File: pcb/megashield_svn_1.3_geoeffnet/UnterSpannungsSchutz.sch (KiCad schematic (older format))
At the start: 15 parts, among them P20 Button, Q3 IRF9540N, Q4 BC337

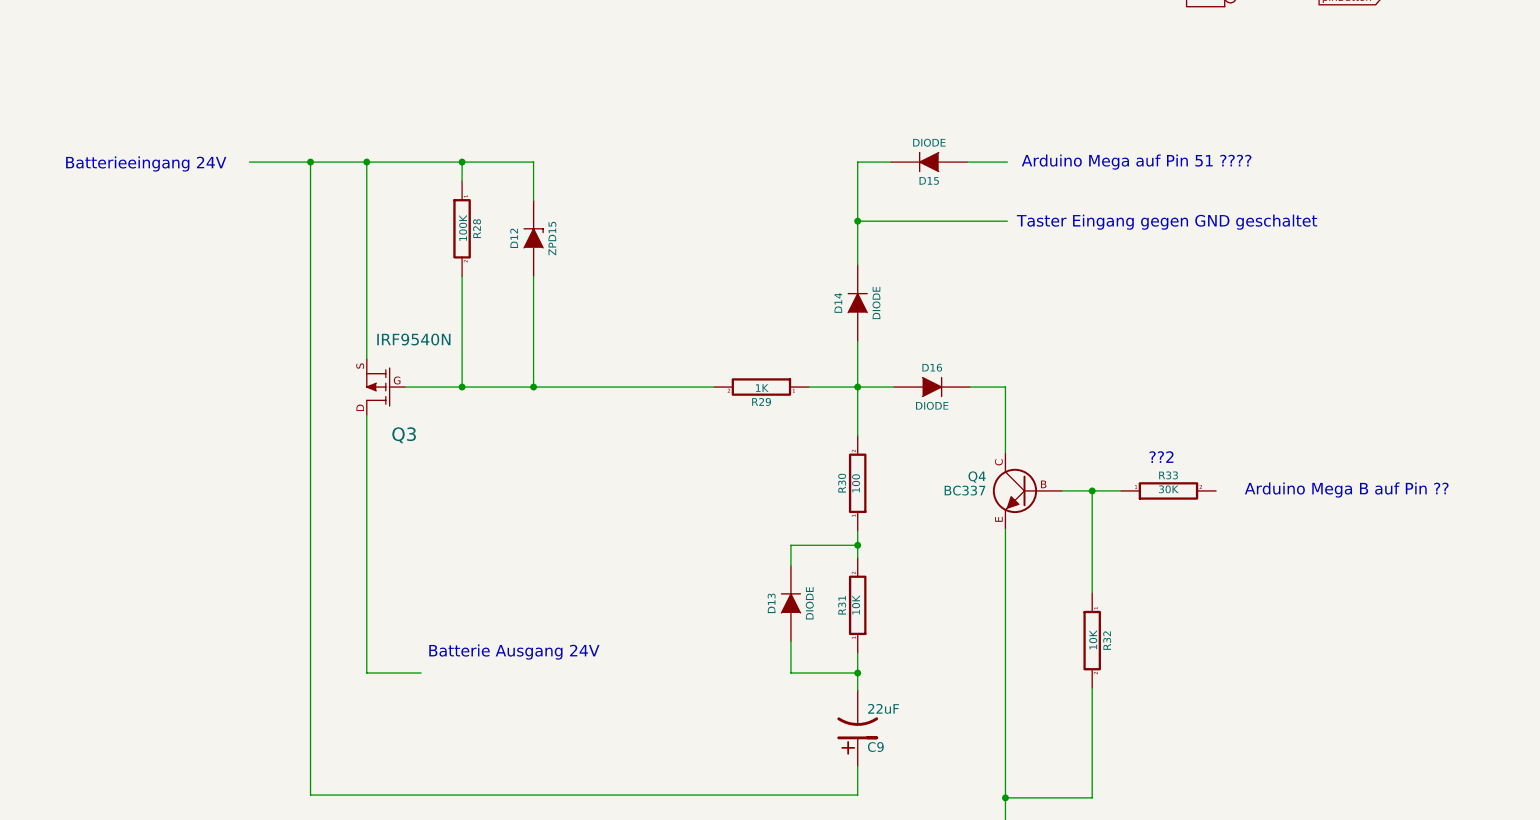
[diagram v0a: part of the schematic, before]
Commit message: Platine V1.3
Hierarchischer Schaltplan für Step Down Wandler erstellt
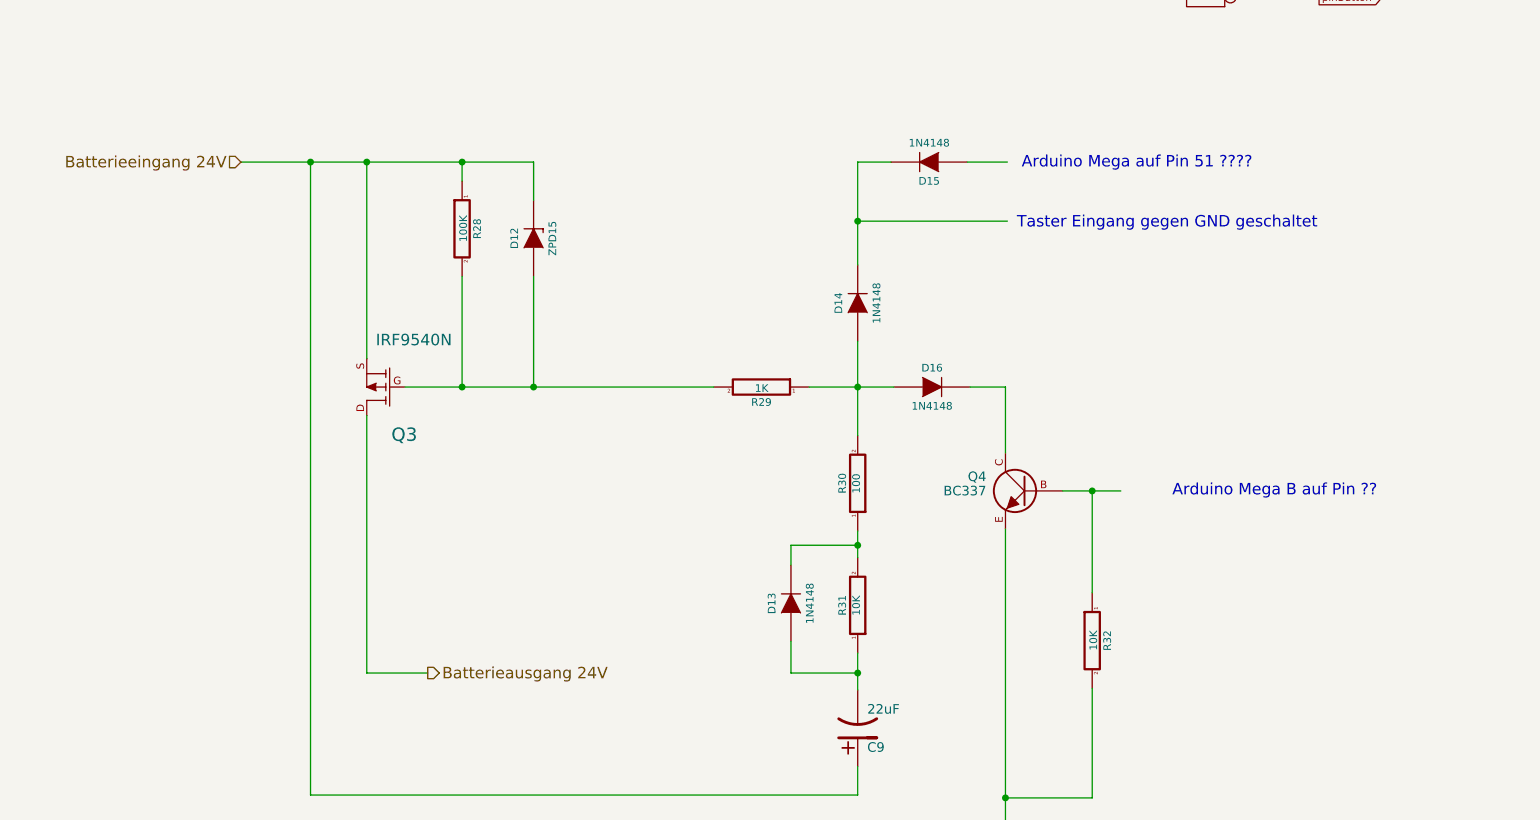
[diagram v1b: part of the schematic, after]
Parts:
- removed R33: 30K, symbol R
- D13, D14, D15, D16: value DIODE -> 1N4148
- P20: footprint (none) -> ACS712:Pin_Header_Straight_1x02
- Q4: footprint TO-92 -> (none)
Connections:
- net labels added: Batterieausgang 24V, Batterieeingang 24V
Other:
- note removed: "??2"
- note removed: "Batterie Ausgang 24V"
- note removed: "Batterieeingang 24V"
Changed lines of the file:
@@
 EESchema Schematic File Version 2
+LIBS:Lötpad_2,5mm
 LIBS:power
 LIBS:Bluetooth_ZS_HC_05
@@
 $Descr A4 11693 8268
 encoding utf-8
-Sheet 3 16
+Sheet 3 17
 Title "Ardumower shield SVN Version 1.3"
 Date "Sonntag, 26. April 2015"
 Rev "1.3"
-Comp " by UweZ"
-Comment1 ""
+Comp "von UweZ"
+Comment1 "Unterspannungsschutz von AlexanderG"
 Comment2 ""
 Comment3 ""
@@
 F 0 "Q3" H 4173 3470 70  0000 C CNN
 F 1 "IRF9540N" H 4123 2973 60  0000 C CNN
-F 2 "" H 4270 3220 60  0000 C CNN
+F 2 "" H 4270 3220 60  0001 C CNN
 F 3 "" H 4270 3220 60  0000 C CNN
 	1    4270 3220
@@
 F 0 "R28" V 4750 2390 40  0000 C CNN
 F 1 "100K" V 4677 2391 40  0000 C CNN
-F 2 "" V 4600 2390 30  0000 C CNN
+F 2 "" V 4600 2390 30  0001 C CNN
 F 3 "" H 4670 2390 30  0000 C CNN
 F 4 "Value" H 4670 2390 60  0001 C CNN "Bestellnummer"
@@
 F 0 "D12" H 5045 2540 40  0000 C CNN
 F 1 "ZPD15" H 5045 2340 40  0000 C CNN
-F 2 "" H 5045 2440 60  0000 C CNN
+F 2 "" H 5045 2440 60  0001 C CNN
 F 3 "" H 5045 2440 60  0000 C CNN
 	1    5045 2440
@@
 F 0 "R29" V 6320 3220 40  0000 C CNN
 F 1 "1K" V 6247 3221 40  0000 C CNN
-F 2 "" V 6170 3220 30  0000 C CNN
+F 2 "" V 6170 3220 30  0001 C CNN
 F 3 "" H 6240 3220 30  0000 C CNN
 F 4 "Value" H 6240 3220 60  0001 C CNN "Bestellnummer"
@@
 P 6745 2780
 F 0 "D14" H 6745 2880 40  0000 C CNN
-F 1 "DIODE" H 6745 2680 40  0000 C CNN
-F 2 "" H 6745 2780 60  0000 C CNN
+F 1 "1N4148" H 6745 2680 40  0000 C CNN
+F 2 "" H 6745 2780 60  0001 C CNN
 F 3 "" H 6745 2780 60  0000 C CNN
 	1    6745 2780
@@
 P 7135 3220
 F 0 "D16" H 7135 3320 40  0000 C CNN
-F 1 "DIODE" H 7135 3120 40  0000 C CNN
-F 2 "" H 7135 3220 60  0000 C CNN
+F 1 "1N4148" H 7135 3120 40  0000 C CNN
+F 2 "" H 7135 3220 60  0001 C CNN
 F 3 "" H 7135 3220 60  0000 C CNN
 	1    7135 3220
@@
 P 7120 2040
 F 0 "D15" H 7120 2140 40  0000 C CNN
-F 1 "DIODE" H 7120 1940 40  0000 C CNN
-F 2 "" H 7120 2040 60  0000 C CNN
+F 1 "1N4148" H 7120 1940 40  0000 C CNN
+F 2 "" H 7120 2040 60  0001 C CNN
 F 3 "" H 7120 2040 60  0000 C CNN
 	1    7120 2040
@@
 F 0 "R30" V 6825 3725 40  0000 C CNN
 F 1 "100" V 6752 3726 40  0000 C CNN
-F 2 "" V 6675 3725 30  0000 C CNN
+F 2 "" V 6675 3725 30  0001 C CNN
 F 3 "" H 6745 3725 30  0000 C CNN
 	1    6745 3725
@@
 F 0 "Q4" H 7820 3840 50  0000 L CNN
 F 1 "BC337" H 7820 3765 50  0000 L CNN
-F 2 "TO-92" H 7820 3690 50  0001 L CIN
+F 2 "" H 7820 3690 50  0001 L CIN
 F 3 "" H 7620 3765 50  0000 L CNN
 	1    7620 3765
 	-1   0    0    -1
-$EndComp
-$Comp
-L R R33
-U 1 1 553A7597
-P 8375 3765
-F 0 "R33" V 8455 3765 40  0000 C CNN
-F 1 "30K" V 8382 3766 40  0000 C CNN
-F 2 "" V 8305 3765 30  0000 C CNN
-F 3 "" H 8375 3765 30  0000 C CNN
-	1    8375 3765
-	0    -1   -1   0
 $EndComp
 $Comp
@@
 F 0 "R32" V 8055 4550 40  0000 C CNN
 F 1 "10K" V 7982 4551 40  0000 C CNN
-F 2 "" V 7905 4550 30  0000 C CNN
+F 2 "" V 7905 4550 30  0001 C CNN
 F 3 "" H 7975 4550 30  0000 C CNN
 	1    7975 4550
@@
 F 0 "R31" V 6825 4365 40  0000 C CNN
 F 1 "10K" V 6752 4366 40  0000 C CNN
-F 2 "" V 6675 4365 30  0000 C CNN
+F 2 "" V 6675 4365 30  0001 C CNN
 F 3 "" H 6745 4365 30  0000 C CNN
 F 4 "Value" H 6745 4365 60  0001 C CNN "Bestellnummer"
@@
 P 6395 4355
 F 0 "D13" H 6395 4455 40  0000 C CNN
-F 1 "DIODE" H 6395 4255 40  0000 C CNN
-F 2 "" H 6395 4355 60  0000 C CNN
+F 1 "1N4148" H 6395 4255 40  0000 C CNN
+F 2 "" H 6395 4355 60  0001 C CNN
 F 3 "" H 6395 4355 60  0000 C CNN
 	1    6395 4355
@@
 F 0 "C9" H 6795 5110 50  0000 L CNN
 F 1 "22uF" H 6795 4910 50  0000 L CNN
-F 2 "" H 6745 5010 60  0000 C CNN
+F 2 "" H 6745 5010 60  0001 C CNN
 F 3 "" H 6745 5010 60  0000 C CNN
 F 4 "Value" H 6745 5010 60  0001 C CNN "Bestellnummer"
@@
 $EndComp
 $Comp
-L GND #PWR037
+L GND #PWR024
 U 1 1 553A83F5
 P 7520 5580
-F 0 "#PWR037" H 7520 5330 60  0001 C CNN
+F 0 "#PWR024" H 7520 5330 60  0001 C CNN
 F 1 "GND" H 7520 5430 60  0000 C CNN
 F 2 "" H 7520 5580 60  0000 C CNN
@@
 	1    0    0    -1
 $EndComp
-Text Notes 4490 4650 0    60   ~ 0
-Batterie Ausgang 24V
-Text Notes 2585 2090 0    60   ~ 0
-Batterieeingang 24V
 Text Notes 7580 2395 0    60   ~ 0
 Taster Eingang gegen GND geschaltet
 Text Notes 7605 2080 0    60   ~ 0
 Arduino Mega auf Pin 51 ????
-Text Notes 8270 3635 0    60   ~ 0
-??2
-Text Notes 8775 3800 0    60   ~ 0
+Text Notes 8395 3800 0    60   ~ 0
 Arduino Mega B auf Pin ??
 Wire Wire Line
@@
 	4670 2040 4670 2140
 Wire Wire Line
-	3555 2040 5045 2040
+	3510 2040 5045 2040
 Wire Wire Line
 	5045 2040 5045 2240
@@
 	4170 3370 4170 4720
 Wire Wire Line
-	4170 4720 4455 4720
+	4170 4720 4490 4720
 Connection ~ 3875 2040
 Wire Wire Line
@@
 F 0 "P20" V 8520 1075 40  0000 C CNN
 F 1 "Button" V 8620 1075 40  0000 C CNN
-F 2 "" H 8570 1075 60  0000 C CNN
+F 2 "ACS712:Pin_Header_Straight_1x02" H 8570 1075 60  0001 C CNN
 F 3 "" H 8570 1075 60  0000 C CNN
 F 4 "Value" H 8570 1075 60  0001 C CNN "Bestellnummer"
@@
 $EndComp
 $Comp
-L GND #PWR038
+L GND #PWR025
 U 1 1 553E5900
 P 9165 975
-F 0 "#PWR038" H 9165 725 60  0001 C CNN
+F 0 "#PWR025" H 9165 725 60  0001 C CNN
 F 1 "GND" V 9165 760 60  0000 C CNN
 F 2 "" H 9165 975 60  0000 C CNN
@@
 Wire Wire Line
 	8920 1175 9165 1175
+Text HLabel 3510 2040 0    60   Input ~ 0
+Batterieeingang 24V
+Text HLabel 4490 4720 2    60   Output ~ 0
+Batterieausgang 24V
 $EndSCHEMATC

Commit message: Platine V1.3 - 1 Schaltplanentwurf
nur Schaltplan gezeichnet nichts an der Platine
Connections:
- net labels added: Ausschalter, PinButton
- net labels removed: pinButton
- wire segments 33 -> 32
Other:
- moved on the sheet: D15, P20
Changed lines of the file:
@@
 $Descr A4 11693 8268
 encoding utf-8
-Sheet 3 17
+Sheet 16 17
 Title "Ardumower shield SVN Version 1.3"
 Date "Sonntag, 26. April 2015"
@@
 L DIODE D15
 U 1 1 553A6F4A
-P 7120 2040
-F 0 "D15" H 7120 2140 40  0000 C CNN
-F 1 "1N4148" H 7120 1940 40  0000 C CNN
-F 2 "" H 7120 2040 60  0001 C CNN
-F 3 "" H 7120 2040 60  0000 C CNN
-	1    7120 2040
+P 7120 1515
+F 0 "D15" H 7120 1615 40  0000 C CNN
+F 1 "1N4148" H 7120 1415 40  0000 C CNN
+F 2 "" H 7120 1515 60  0001 C CNN
+F 3 "" H 7120 1515 60  0000 C CNN
+	1    7120 1515
 	-1   0    0    1
 $EndComp
@@
 	1    0    0    -1
 $EndComp
-Text Notes 7580 2395 0    60   ~ 0
+Text Notes 8300 2305 0    60   ~ 0
 Taster Eingang gegen GND geschaltet
-Text Notes 7605 2080 0    60   ~ 0
+Text Notes 8250 1555 0    60   ~ 0
 Arduino Mega auf Pin 51 ????
-Text Notes 8395 3800 0    60   ~ 0
+Text Notes 9175 3820 0    60   ~ 0
 Arduino Mega B auf Pin ??
 Wire Wire Line
@@
 	7520 3220 7520 3565
 Wire Wire Line
-	7820 3765 8125 3765
+	7820 3765 8265 3765
 Wire Wire Line
 	7975 4300 7975 3765
@@
 Connection ~ 3875 2040
 Wire Wire Line
-	6745 2040 6745 2580
-Wire Wire Line
-	7530 2350 6745 2350
+	6745 1515 6745 2580
+Wire Wire Line
+	6745 2350 7890 2350
 Connection ~ 6745 2350
 Connection ~ 5045 3220
 Connection ~ 4670 3220
 Wire Wire Line
-	6920 2040 6745 2040
-Wire Wire Line
-	7320 2040 7530 2040
+	6920 1515 6745 1515
+Wire Wire Line
+	7320 1515 7530 1515
 $Comp
 L CONN_2 P20
 U 1 1 553E561A
-P 8570 1075
-F 0 "P20" V 8520 1075 40  0000 C CNN
-F 1 "Button" V 8620 1075 40  0000 C CNN
-F 2 "ACS712:Pin_Header_Straight_1x02" H 8570 1075 60  0001 C CNN
-F 3 "" H 8570 1075 60  0000 C CNN
-F 4 "Value" H 8570 1075 60  0001 C CNN "Bestellnummer"
-	1    8570 1075
-	-1   0    0    1
+P 7990 2000
+F 0 "P20" V 7940 2000 40  0000 C CNN
+F 1 "Button" V 8040 2000 40  0000 C CNN
+F 2 "ACS712:Pin_Header_Straight_1x02" H 7990 2000 60  0001 C CNN
+F 3 "" H 7990 2000 60  0000 C CNN
+F 4 "Value" H 7990 2000 60  0001 C CNN "Bestellnummer"
+	1    7990 2000
+	0    -1   -1   0
 $EndComp
 $Comp
 L GND #PWR025
 U 1 1 553E5900
-P 9165 975
-F 0 "#PWR025" H 9165 725 60  0001 C CNN
-F 1 "GND" V 9165 760 60  0000 C CNN
-F 2 "" H 9165 975 60  0000 C CNN
-F 3 "" H 9165 975 60  0000 C CNN
-	1    9165 975
-	0    -1   -1   0
-$EndComp
-Wire Wire Line
-	8920 975  9165 975
-Text GLabel 9165 1175 2    39   Output ~ 0
-pinButton
-Wire Wire Line
-	8920 1175 9165 1175
+P 8090 2595
+F 0 "#PWR025" H 8090 2345 60  0001 C CNN
+F 1 "GND" V 8090 2380 60  0000 C CNN
+F 2 "" H 8090 2595 60  0000 C CNN
+F 3 "" H 8090 2595 60  0000 C CNN
+	1    8090 2595
+	1    0    0    -1
+$EndComp
+Wire Wire Line
+	8090 2350 8090 2595
 Text HLabel 3510 2040 0    60   Input ~ 0
 Batterieeingang 24V
 Text HLabel 4490 4720 2    60   Output ~ 0
 Batterieausgang 24V
+Text HLabel 7530 1515 2    60   Output ~ 0
+PinButton
+Text HLabel 8265 3765 2    60   Input ~ 0
+Ausschalter
 $EndSCHEMATC

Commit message: Platine V1.3
Grundgerüst fertig
LED Schaltung muss noch geändert werden und RC Änderung
Bauteil Bezeichnungen, Schaltplan; Abmessungen und Duoadapter müssen
überprüft werden.
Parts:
- added R35: 30K, ACS712:Resistor_Horizontal_RM10mm, symbol R
- C9: footprint (none) -> ACS712:Elko_vert_11.2x6.3mm_RM2.5_RM5.0
- D13, D16: value 1N4148 -> 1N5819; footprint (none) -> ACS712:Diode_ligend_RM10; Bestellnummer (none) -> R: 1N 5819; Technische Daten (none) -> Schottky Diode, DO41, 40V, 1A
- D14, D15: footprint (none) -> ACS712:Diode_ligend_RM10
- Q3: footprint (none) -> Transistors_TO-220:TO-220_FET-GDS_Vertical
- Q4: footprint (none) -> ACS712:TO92-EBC
- R28, R29, R30, R31, R32: footprint (none) -> ACS712:Resistor_Horizontal_RM10mm
- ZD6: renamed from D12; footprint (none) -> ACS712:Diode_ligend_RM10
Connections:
- net Ausschalter: now also R35.2; no longer Q4.B, R32.1
- new net: Q4.B, R32.1, R35.1
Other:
- note added: "1x IRF9540N P-MOSFET T1 (or IRF5210)\n1x BC337 NPN T2\n1x Zener Diode 15V ZD15 Z1\n2x Diode 1N4148 D2, D3\n2x Diode 1N5819 50V D1, D4\n1x 22 uF C1\n1x 1k R4\n2x 10k (R3, R8)\n1x 30k R6\n2x 100k (R2, R7)"
- note added: "Arduino Mega B auf Pin 4"
- note added: "beim flashen über usb wird der akku getrennt (alle pins gehen auf hochomig) - das sollte aber kein problem sein (usb versorgung des arduinos) - beim programmstart wird der akku dann wieder zugeschaltet"
- note added: "vielleicht schreibst du noch bei was die teilschaltungen machen sollen\n[00:05:52] Alexander Grau: zener diode z.b. soll Ugs auf -15 volt begrenzen\n[00:06:31] Alexander Grau: C9 und D13 sollen über R31, R30 eine verzögerungsschaltung bilden\n[00:06:39] Alexander Grau: (für eine richtung)\n[00:07:27] Alexander Grau: beim pmos evtl. noch beschreiben wann er schaltet und wann nicht:\n[00:07:37] Ale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"
- note removed: "Arduino Mega B auf Pin ??"
